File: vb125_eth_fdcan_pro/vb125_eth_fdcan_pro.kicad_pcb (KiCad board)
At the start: 6 copper layers, 96 x 82 mm, 325 parts, among them J1 MEM2061-01-188-00-A, J2 TAGconnect NL, J4 ARJM11D7-114-AB, J5 USB_C_Receptacle_USB2.0, J6 D09P33E4GL00LF, J7 D09P33E4GL00LF, K1 EE2-4.5TNUH, K2 EE2-4.5TNUH, M1 DM-OLED042-647, M2 B0505MT-1WR4, M3 B0505MT-1WR4, Q1 BSS138, Q2 BSS138, Q3 BSS138, Q4 BSS138, Q5 MMBTA42, Q6 Si3440DV, Q7 2N7002, T1 PA1134NL, T2 750315125, U1 STM32H725IGKx, U10 TLP2270, U11 LTC4267, U12 PS2911-1-F3-AX, U13 ZR431, U15 LT8304IS8E#PBF, U2 LAN8740A, U3 NCP563SQ18T1G, U4 USB3315, U5 AOZ1376DI-02, U6 RT5760A/B, U7 ADM3050EBRIZ, U8 TLP2270, U9 ADM3050EBRIZ, X1 ECX-.327-CDX-1293, X2 50MHz, X3 24MHz

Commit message: Update vb125_eth_fdcan_pro.kicad_pcb
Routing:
- net /CAN Ch1/FDCAN_TX: track 17.9 -> 18.5 mm
- net /CAN Ch1/FDCAN_RX: track 17.9 -> 18.4 mm

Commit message: Update sch and pcb.
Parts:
- removed C66, C80, C93: Y rated, SMD 1808, vhrd_generic:C_1808_4520Metric
- added E1: SparkGap, vhrd_generic:SPARK_GAP_011, F.Cu at (180.4, 81.5)
- added E2: SparkGap, vhrd_generic:SPARK_GAP_011, F.Cu at (180.4, 116.2)
- added E3: SparkGap, vhrd_generic:SPARK_GAP_011, F.Cu at (180.4, 84.0)
- added E4: SparkGap, vhrd_generic:SPARK_GAP_011, F.Cu at (180.4, 118.5)
- added E5: SparkGap, vhrd_generic:SPARK_GAP_011, F.Cu at (187.1, 76.6)
- added JP1: SolderJumper_2_Open, Jumper:SolderJumper-2_P1.3mm_Open_RoundedPad1.0x1.5mm, B.Cu at (182.0, 72.2)
- added JP2: SolderJumper_2_Open, Jumper:SolderJumper-2_P1.3mm_Open_RoundedPad1.0x1.5mm, B.Cu at (182.0, 107.0)
- C65, C79, C92: footprint Capacitor_THT:C_Disc_D7.0mm_W2.5mm_P5.00mm -> vhrd_generic:C_Disc_D7.0mm_W2.5mm_P6.00mm
- moved TP17 7.40 mm to (187.0, 82.1)
- moved TP21 7.30 mm to (186.9, 116.7)
- moved TP22 1.22 mm to (179.9, 118.0)
- moved TP18 1.22 mm to (179.9, 83.4)
- moved NT1 0.66 mm to (111.7, 85.2)
- moved C92 0.20 mm to (140.0, 73.0)
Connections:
- J6 pad 5: unconnected-(J6-Pad5) -> Net-(JP1-B)
- J7 pad 5: unconnected-(J7-Pad5) -> Net-(JP2-B)
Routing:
- net CHASSIS: track 4.20 -> 12.3 mm, vias 10 -> 20
- net GND: track 157.9 -> 150.7 mm, vias 186 -> 189
- net /MCU_H7/BOOT0: track 44.2 -> 48.3 mm
- net /CAN Ch2/ISO: track 19.6 -> 17.2 mm
- net ISO_POE: track 17.3 -> 14.9 mm
- net Net-(JP1-B): track 0.00 -> 2.33 mm
- net ISO_1: track 20.9 -> 18.6 mm
- net Net-(JP2-B): track 0.00 -> 2.18 mm
- net /CAN Ch1/CAN_H: track 34.8 -> 36.4 mm, vias 1 -> 0
- net /CAN Ch1/CAN_L: track 35.4 -> 36.9 mm, vias 1 -> 0
- net /CAN Ch2/CAN_L: track 35.8 -> 37.2 mm, vias 1 -> 0
- net /CAN Ch2/CAN_H: track 30.0 -> 31.3 mm, vias 1 -> 0
- net /MCU_H7/I2C2_SDA: track 50.0 -> 50.9 mm
- net /Bus Power/+VIN_DB9: track 13.6 -> 14.4 mm
- net /Eth/+AVDD_PHY: track 58.0 -> 58.8 mm
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
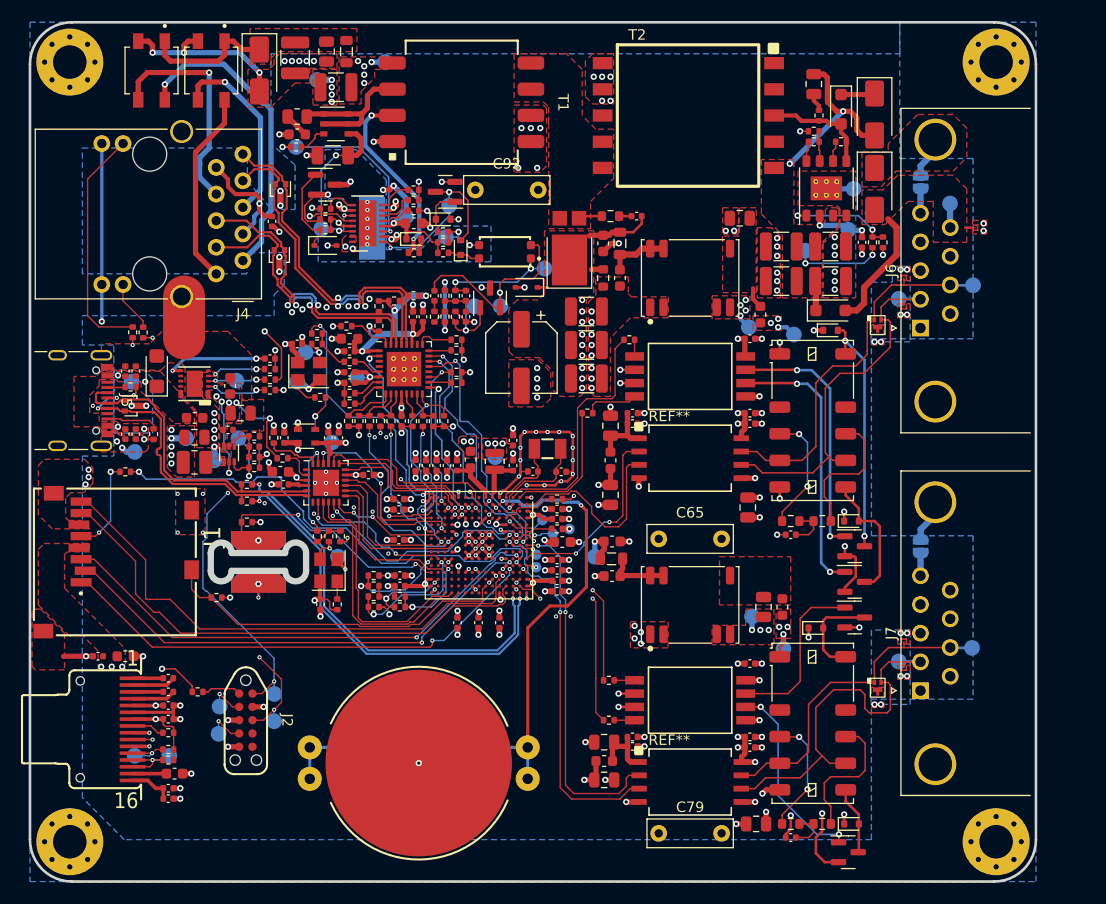
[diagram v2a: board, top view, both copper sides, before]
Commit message: Update outline.
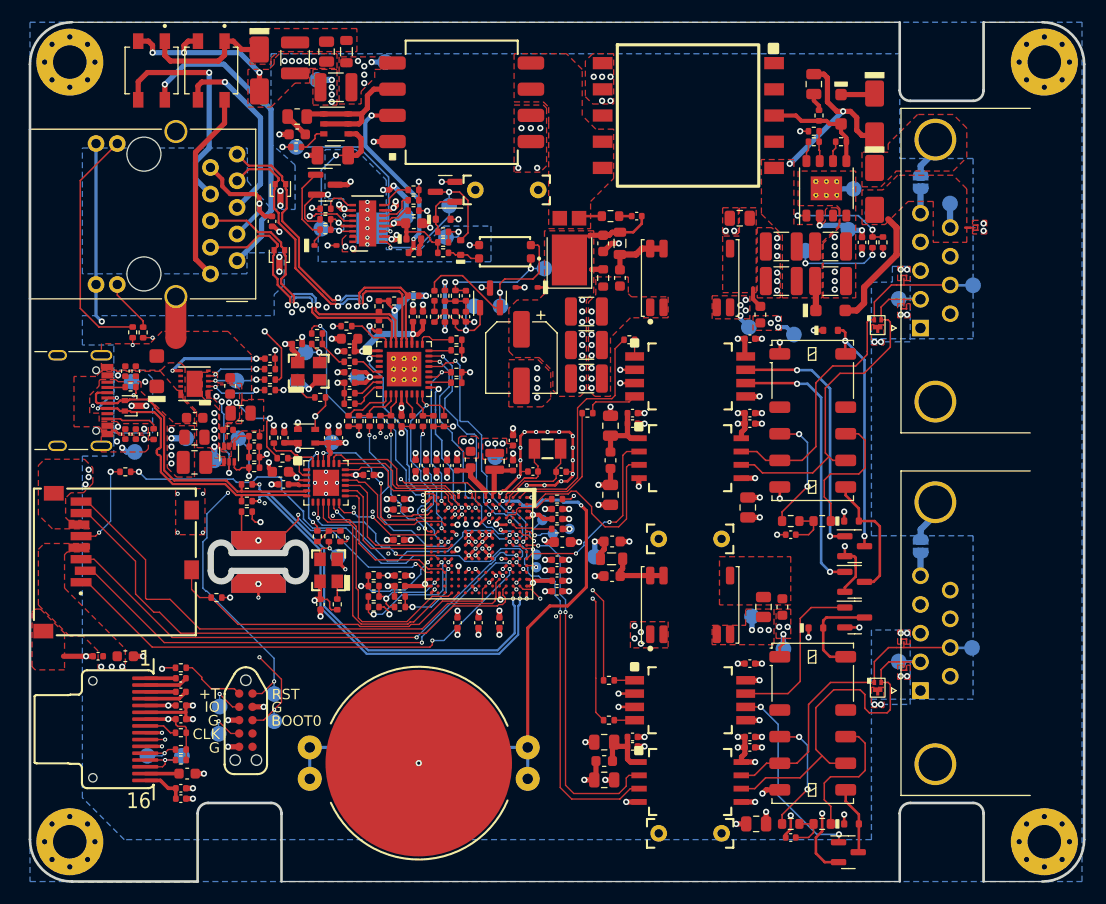
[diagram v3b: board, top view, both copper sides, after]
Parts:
- D11, D17, D19: footprint Diode_SMD:D_SMA -> vhrd_diode:D_SMA
- D12, D23: footprint Diode_SMD:D_SOD-323 -> vhrd_diode:D_SOD-323
- D13, D14, D15, D3, D4, D6, D7: footprint Diode_SMD:D_SOD-523 -> vhrd_diode:D_SOD-523
- D18, D20: footprint Diode_SMD:D_SOD-123F -> vhrd_diode:D_SOD-123F
- D2: footprint Diode_SMD:D_SMF -> vhrd_diode:D_SMF
- X2, X3: footprint Oscillator:Oscillator_SMD_Abracon_ASE-4Pin_3.2x2.5mm -> vhrd_crystal:Oscillator_SMD_Abracon_ASE-4Pin_3.2x2.5mm
- moved H1 4.60 mm to (193.8, 60.8)
- moved H4 4.60 mm to (193.8, 135.2)
- moved R15 2.80 mm to (111.4, 118.6)
- moved C1 1.20 mm to (111.4, 123.5)
- moved C2 1.20 mm to (111.4, 122.2)
- moved C3 1.20 mm to (112.0, 128.7)
- moved C4 1.20 mm to (111.4, 130.1)
- moved C5 1.20 mm to (111.4, 131.1)
- moved C6 1.20 mm to (111.4, 119.6)
- moved C7 1.20 mm to (111.4, 120.9)
- moved M1 1.20 mm to (108.0, 124.5)
- moved R1 1.20 mm to (111.4, 127.4)
- moved R2 1.20 mm to (111.4, 126.4)
- moved R7 1.20 mm to (111.4, 124.8)
- moved TP1 1.20 mm to (108.2, 127.0)
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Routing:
- net Net-(J2-Pad1): track 3.77 -> 6.19 mm
- net +3V3_DCDC: track 79.9 -> 77.9 mm
- net /Eth/+AVDD_PHY: track 58.8 -> 59.5 mm
- net GND: track 150.7 -> 151.4 mm
- net /MCU_H7/I2C2_SCL: track 48.1 -> 48.7 mm
- net /Eth/RD_N: track 28.7 -> 29.2 mm
- net /Eth/TD_P: track 33.1 -> 33.7 mm
- net /Eth/TD_N: track 33.8 -> 34.4 mm
- net /Eth/RD_P: track 28.1 -> 28.6 mm
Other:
- board size 96 x 82 mm -> 100.6 x 82 mm
- board text added: "+T"
- board text added: "BOOT0"
- board text added: "CLK"
- board text added: "G"
- board text added: "IO"
- board text added: "RST"
